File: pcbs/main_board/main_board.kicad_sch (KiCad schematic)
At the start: 2 parts, among them U1 mini_esp32, U2 ADXL345

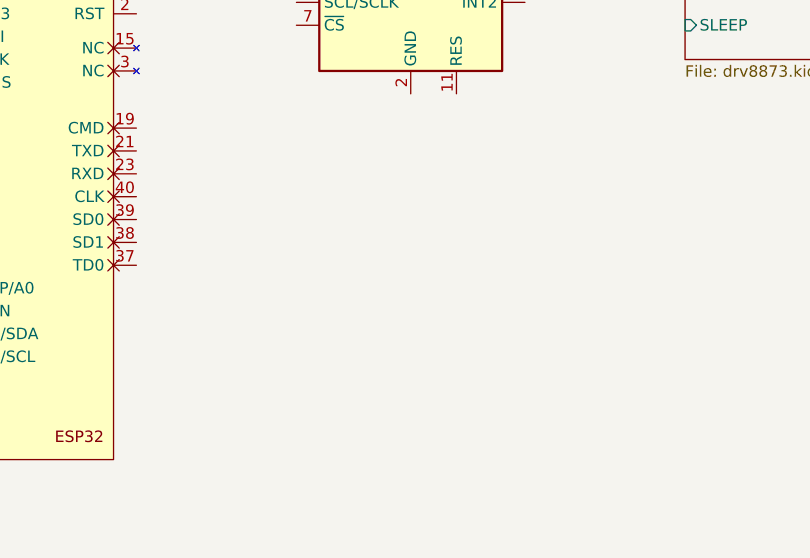
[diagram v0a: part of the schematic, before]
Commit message: Add display footprint, symbol
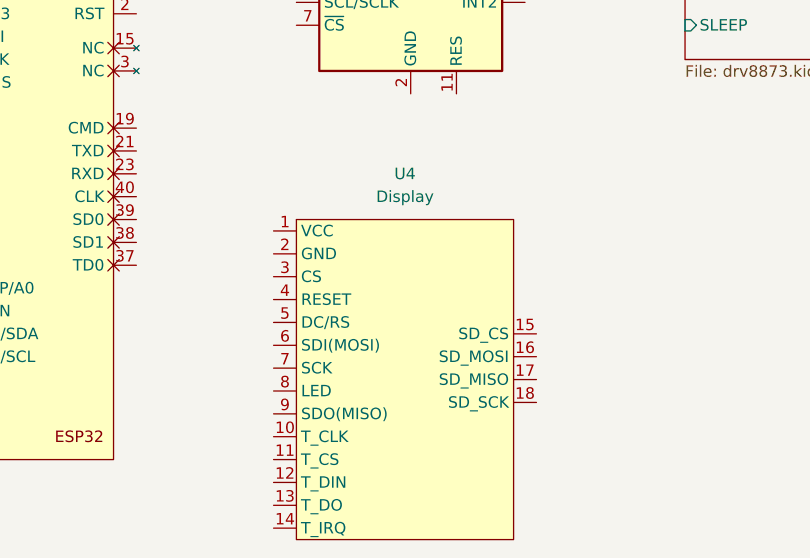
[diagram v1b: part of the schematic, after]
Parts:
- added U4: Display, display:display_footprint, symbol display_sym:display
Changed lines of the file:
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@@
 	(paper "A4")
+	(symbol
+		(lib_id "display_sym:display")
+		(at 99.06 88.9 0)
+		(unit 1)
+		(exclude_from_sim no)
+		(in_bom yes)
+		(on_board yes)
+		(dnp no)
+		(fields_autoplaced yes)
+		(property "Reference" "U4"
+			(at 98.425 67.31 0)
+			(effects
+				(font
+					(size 1.27 1.27)
+				)
+			)
+		)
+		(property "Value" "Display"
+			(at 98.425 69.85 0)
+			(effects
+				(font
+					(size 1.27 1.27)
+				)
+			)
+		)
+		(property "Footprint" "display:display_footprint"
+			(at 99.06 88.9 0)
+			(effects
+				(font
+					(size 1.27 1.27)
+				)
+				(hide yes)
+			)
+		)
+		(property "Datasheet" "https://www.lcdwiki.com/4.0inch_SPI_Module_ST7796"
+			(at 99.06 88.9 0)
+			(effects
+				(font
+					(size 1.27 1.27)
+				)
+				(hide yes)
+			)
+		)
+		(property "Description" "Display 4 inch"
+			(at 99.06 88.9 0)
+			(effects
+				(font
+					(size 1.27 1.27)
+				)
+				(hide yes)
+			)
+		)
+		(property "Manufacturer Part Number" "LA141073"
+			(at 99.06 88.9 0)
+			(effects
+				(font
+					(size 1.27 1.27)
+				)
+				(hide yes)
+			)
+		)
+		(property "Supplier" "LaskaKit"
+			(at 99.06 88.9 0)
+			(effects
+				(font
+					(size 1.27 1.27)
+				)
+				(hide yes)
+			)
+		)
+		(property "Supplier Part Number" "LA141073"
+			(at 99.06 88.9 0)
+			(effects
+				(font
+					(size 1.27 1.27)
+				)
+				(hide yes)
+			)
+		)
+		(pin "4"
+		)
+		(pin "9"
+		)
+		(pin "12"
+		)
+		(pin "14"
+		)
+		(pin "16"
+		)
+		(pin "2"
+		)
+		(pin "6"
+		)
+		(pin "8"
+		)
+		(pin "10"
+		)
+		(pin "1"
+		)
+		(pin "3"
+		)
+		(pin "5"
+		)
+		(pin "7"
+		)
+		(pin "11"
+		)
+		(pin "13"
+		)
+		(pin "15"
+		)
+		(pin "18"
+		)
+		(pin "17"
+		)
+		(instances
+			(project ""
+				(path "/86b00c07-962a-4c6d-8d05-813891e412c9"
+					(reference "U4")
+					(unit 1)
+				)
+			)
+		)
+	)
 	(symbol
 		(lib_id "Sensor_Motion:ADXL343")

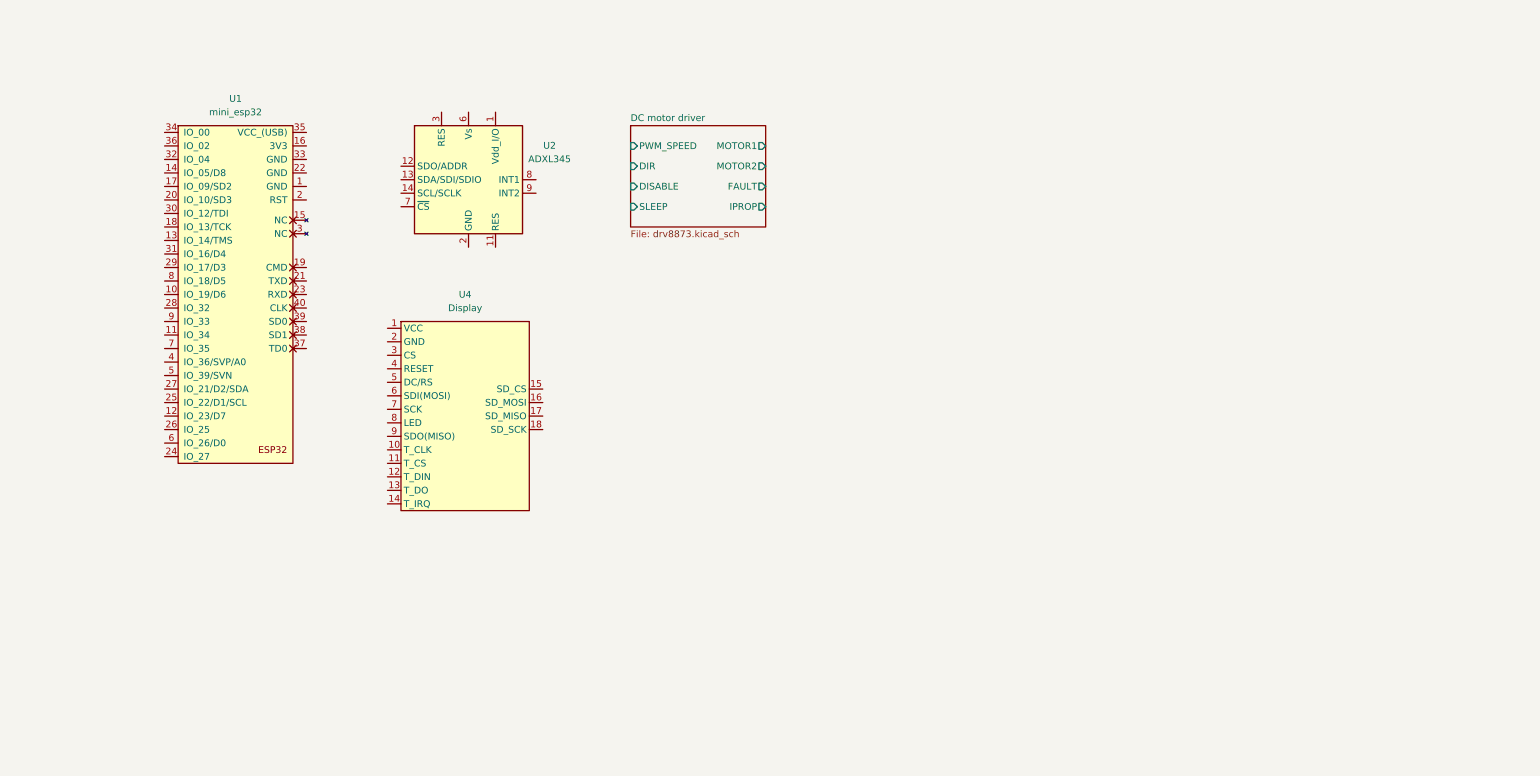
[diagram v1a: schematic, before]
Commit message: Add power distribution sheet
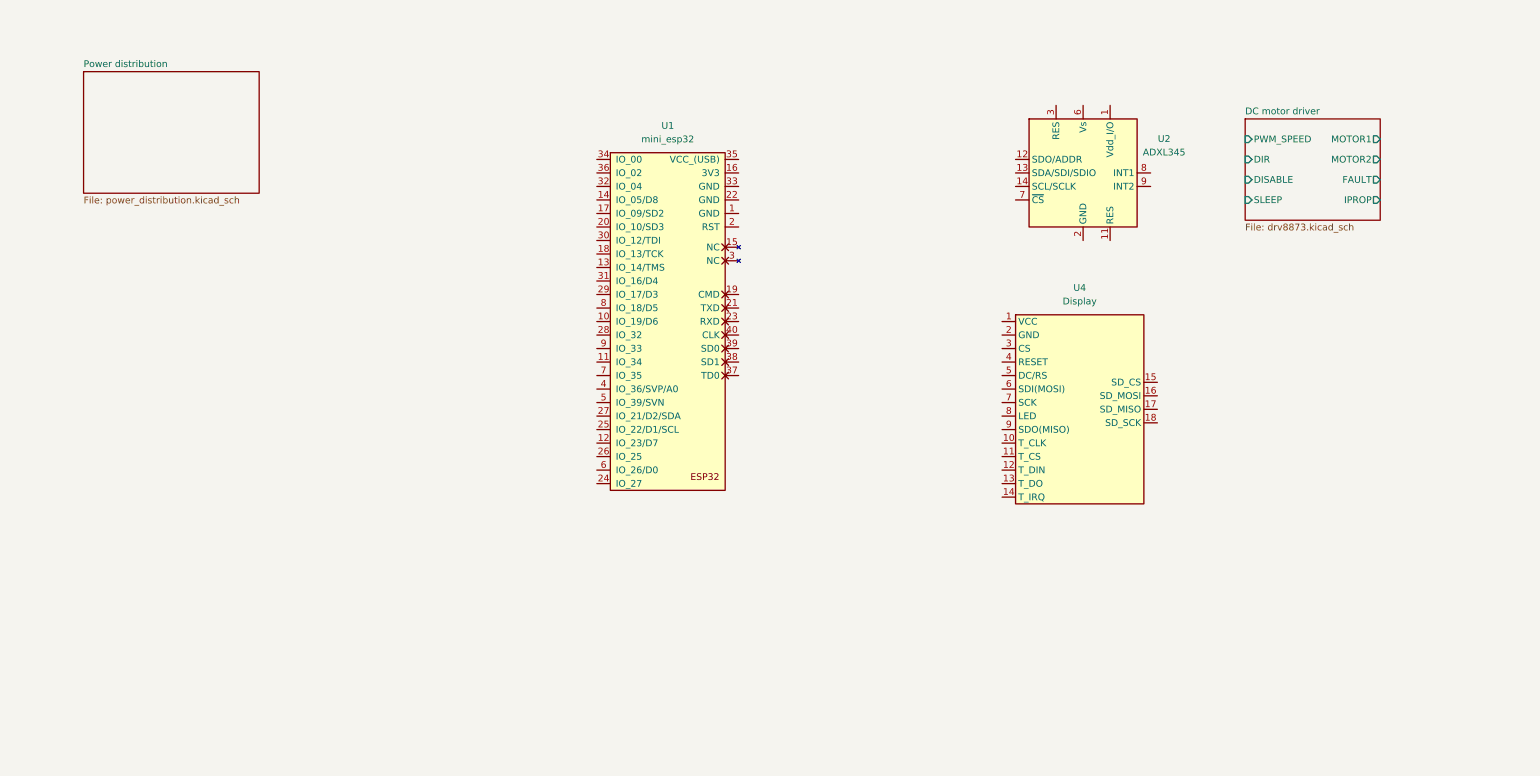
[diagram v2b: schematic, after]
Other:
- added sheet Power distribution (power_distribution.kicad_sch)
- moved on the sheet: U1, U2, U4
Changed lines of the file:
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@@
 	(symbol
 		(lib_id "display_sym:display")
-		(at 99.06 88.9 0)
+		(at 214.63 87.63 0)
 		(unit 1)
 		(exclude_from_sim no)
@@
 		(fields_autoplaced yes)
 		(property "Reference" "U4"
-			(at 98.425 67.31 0)
+			(at 213.995 66.04 0)
 			(effects
 				(font
@@
 		)
 		(property "Value" "Display"
-			(at 98.425 69.85 0)
+			(at 213.995 68.58 0)
 			(effects
 				(font
@@
 		)
 		(property "Footprint" "display:display_footprint"
-			(at 99.06 88.9 0)
+			(at 214.63 87.63 0)
 			(effects
 				(font
@@
 		)
 		(property "Datasheet" "https://www.lcdwiki.com/4.0inch_SPI_Module_ST7796"
-			(at 99.06 88.9 0)
+			(at 214.63 87.63 0)
 			(effects
 				(font
@@
 		)
 		(property "Description" "Display 4 inch"
-			(at 99.06 88.9 0)
+			(at 214.63 87.63 0)
 			(effects
 				(font
@@
 		)
 		(property "Manufacturer Part Number" "LA141073"
-			(at 99.06 88.9 0)
+			(at 214.63 87.63 0)
 			(effects
 				(font
@@
 		)
 		(property "Supplier" "LaskaKit"
-			(at 99.06 88.9 0)
+			(at 214.63 87.63 0)
 			(effects
 				(font
@@
 		)
 		(property "Supplier Part Number" "LA141073"
-			(at 99.06 88.9 0)
+			(at 214.63 87.63 0)
 			(effects
 				(font
@@
 	(symbol
 		(lib_id "Sensor_Motion:ADXL343")
-		(at 99.06 45.72 0)
+		(at 214.63 44.45 0)
 		(unit 1)
 		(exclude_from_sim no)
@@
 		(fields_autoplaced yes)
 		(property "Reference" "U2"
-			(at 114.3 39.2998 0)
+			(at 229.87 38.0298 0)
 			(effects
 				(font
@@
 		)
 		(property "Value" "ADXL345"
-			(at 114.3 41.8398 0)
+			(at 229.87 40.5698 0)
 			(effects
 				(font
@@
 		)
 		(property "Footprint" "Package_LGA:LGA-14_3x5mm_P0.8mm_LayoutBorder1x6y"
-			(at 99.06 45.72 0)
+			(at 214.63 44.45 0)
 			(effects
 				(font
@@
 		)
 		(property "Datasheet" "https://cz.mouser.com/datasheet/3/1014/1/5EB6D493A261F4A83E1FA0AE2BA84ED391EF50A03F09427C365C2A225C2ED909.pdf"
-			(at 99.06 45.72 0)
+			(at 214.63 44.45 0)
 			(effects
 				(font
@@
 		)
 		(property "Description" "3-Axis MEMS Accelerometer"
-			(at 99.06 45.72 0)
+			(at 214.63 44.45 0)
 			(effects
 				(font
@@
 		)
 		(property "Manufacturer Part Number" "ADXL345BCCZ"
-			(at 99.06 45.72 0)
+			(at 214.63 44.45 0)
 			(effects
 				(font
@@
 		)
 		(property "Supplier" "Mouser"
-			(at 99.06 45.72 0)
+			(at 214.63 44.45 0)
 			(effects
 				(font
@@
 		)
 		(property "Supplier Part Number" "584-ADXL345BCCZ"
-			(at 99.06 45.72 0)
+			(at 214.63 44.45 0)
 			(effects
 				(font
@@
 	(symbol
 		(lib_id "ESP32_mini:mini_esp32")
-		(at 54.61 34.29 0)
+		(at 135.89 39.37 0)
 		(unit 1)
 		(exclude_from_sim no)
@@
 		(fields_autoplaced yes)
 		(property "Reference" "U1"
-			(at 55.245 30.48 0)
+			(at 136.525 35.56 0)
 			(effects
 				(font
@@
 		)
 		(property "Value" "mini_esp32"
-			(at 55.245 33.02 0)
+			(at 136.525 38.1 0)
 			(effects
 				(font
@@
 		)
 		(property "Footprint" "ESP32_mini:ESP32_mini"
-			(at 58.42 31.75 0)
+			(at 139.7 36.83 0)
 			(effects
 				(font
@@
 		)
 		(property "Datasheet" "https://www.laskakit.cz/user/related_files/esp32-wroom-32_datasheet_en.pdf"
-			(at 58.42 31.75 0)
+			(at 139.7 36.83 0)
 			(effects
 				(font
@@
 		)
 		(property "Description" "ESP DevKit"
-			(at 54.61 34.29 0)
+			(at 135.89 39.37 0)
 			(effects
 				(font
@@
 		)
 		(property "Manufacturer Part Number" "~"
-			(at 54.61 34.29 0)
+			(at 135.89 39.37 0)
 			(effects
 				(font
@@
 		)
 		(property "Supplier" "LaskaKit"
-			(at 54.61 34.29 0)
+			(at 135.89 39.37 0)
 			(effects
 				(font
@@
 		)
 		(property "Supplier Part Number" "LA100089"
-			(at 54.61 34.29 0)
+			(at 135.89 39.37 0)
 			(effects
 				(font
@@
 	)
 	(sheet
-		(at 129.54 35.56)
+		(at 245.11 34.29)
 		(size 25.4 19.05)
 		(exclude_from_sim no)
@@
 		)
 		(property "Sheetname" "DC motor driver"
-			(at 129.54 34.8484 0)
+			(at 245.11 33.5784 0)
 			(effects
 				(font
@@
 		)
 		(property "Sheetfile" "drv8873.kicad_sch"
-			(at 129.54 55.1946 0)
+			(at 245.11 53.9246 0)
 			(effects
 				(font
@@
 		)
 		(pin "DIR" input
-			(at 129.54 43.18 180)
+			(at 245.11 41.91 180)
 			(effects
 				(font
@@
 		)
 		(pin "DISABLE" input
-			(at 129.54 46.99 180)
+			(at 245.11 45.72 180)
 			(effects
 				(font
@@
 		)
 		(pin "FAULT" output
-			(at 154.94 46.99 0)
+			(at 270.51 45.72 0)
 			(effects
 				(font
@@
 		)
 		(pin "IPROP" output
-			(at 154.94 50.8 0)
+			(at 270.51 49.53 0)
 			(effects
 				(font
@@
 		)
 		(pin "MOTOR1" output
-			(at 154.94 39.37 0)
+			(at 270.51 38.1 0)
 			(effects
 				(font
@@
 		)
 		(pin "MOTOR2" output
-			(at 154.94 43.18 0)
+			(at 270.51 41.91 0)
 			(effects
 				(font
@@
 		)
 		(pin "PWM_SPEED" input
-			(at 129.54 39.37 180)
+			(at 245.11 38.1 180)
 			(effects
 				(font
@@
 		)
 		(pin "SLEEP" input
-			(at 129.54 50.8 180)
+			(at 245.11 49.53 180)
 			(effects
 				(font
@@
 				)
 			)
+		)
+	)
+	(sheet
+		(at 26.67 25.4)
+		(size 33.02 22.86)
+		(exclude_from_sim no)
+		(in_bom yes)
+		(on_board yes)
+		(dnp no)
+		(fields_autoplaced yes)
+		(stroke
+			(width 0.1524)
+			(type solid)
+		)
+		(fill
+			(color 0 0 0 0.0000)
+		)
+		(property "Sheetname" "Power distribution"
+			(at 26.67 24.6884 0)
+			(effects
+				(font
+					(size 1.27 1.27)
+				)
+				(justify left bottom)
+			)
+		)
+		(property "Sheetfile" "power_distribution.kicad_sch"
+			(at 26.67 48.8446 0)
+			(effects
+				(font
+					(size 1.27 1.27)
+				)
+				(justify left top)
+			)
+		)
+		(instances
+			(project "main_board"
+				(path "/86b00c07-962a-4c6d-8d05-813891e412c9"
+					(page "3")
+				)
+			)

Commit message: Display wiring to esp
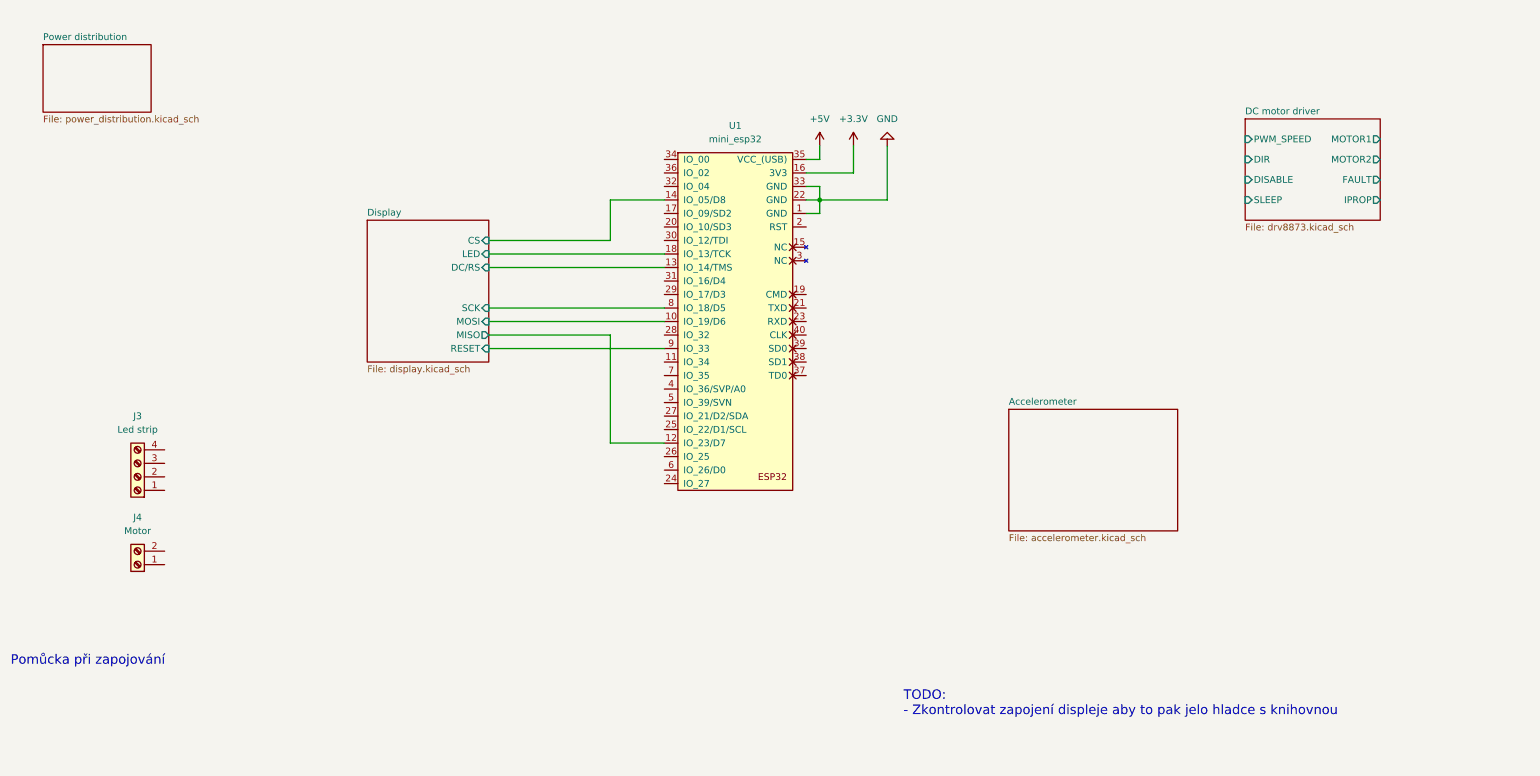
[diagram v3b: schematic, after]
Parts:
- removed U2: ADXL345, Package_LGA:LGA-14_3x5mm_P0.8mm_LayoutBorder1x6y, symbol Sensor_Motion:ADXL343
- removed U4: Display, display:display_footprint, symbol display_sym:display
- added J3: Led strip, symbol Connector:Screw_Terminal_01x04
- added J4: Motor, symbol Connector:Screw_Terminal_01x02
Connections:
- net GND: now reaches U1.1 (GND)
- net GND: now also U1.22 (GND), U1.33 (GND)
- net Display/MOSI: now reaches U1.10 (IO_19/D6)
- net Display/MISO: now reaches U1.12 (IO_23/D7)
- net Display/DC/RS: now reaches U1.13 (IO_14/TMS)
- net Display/CS: now reaches U1.14 (IO_05/D8)
- net +3.3V: now reaches U1.16 (3V3)
- net Display/LED: now reaches U1.18 (IO_13/TCK)
- net +5V: now reaches U1.35 (VCC_(USB))
- net Display/SCK: now reaches U1.8 (IO_18/D5)
- net Display/RESET: now reaches U1.9 (IO_33)
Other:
- added sheet Accelerometer (accelerometer.kicad_sch)
- added sheet Display (display.kicad_sch)
- note added: "Pomůcka při zapojování"
- note added: "TODO: - Zkontrolovat zapojení displeje aby to pak jelo hladce s knihovnou"
- moved on the sheet: U1

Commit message: Add led strip wiring
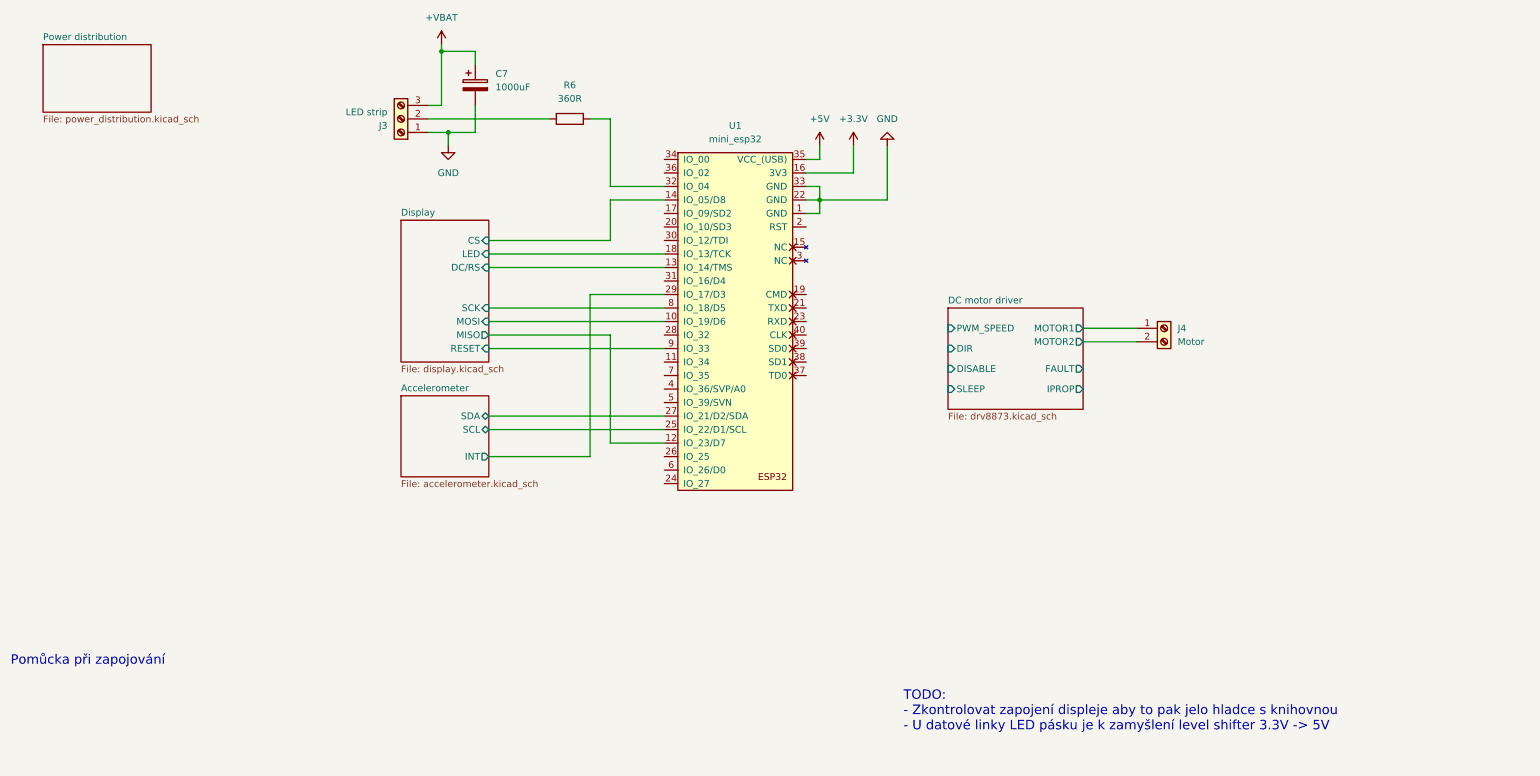
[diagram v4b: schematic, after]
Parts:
- removed J3: Led strip, symbol Connector:Screw_Terminal_01x04
- added C7: 1000uF, symbol Device:C_Polarized
- added J3: LED strip, symbol Connector:Screw_Terminal_01x03
- added R6: 360R, Resistor_SMD:R_0603_1608Metric_Pad0.98x0.95mm_HandSolder, symbol Device:R
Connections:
- net DC motor driver/MOTOR1: now also J4.1 (Pin_1)
- net DC motor driver/MOTOR2: now also J4.2 (Pin_2)
- net GND: now also C7.2, J3.1 (Pin_1)
- net Accelerometer/SCL: now reaches U1.25 (IO_22/D1/SCL)
- net Accelerometer/SDA: now reaches U1.27 (IO_21/D2/SDA)
- net Accelerometer/INT: now reaches U1.29 (IO_17/D3)
- net at U1.32 (IO_04): now also R6.1
- new net: J3.2 (Pin_2), R6.2
- new net +VBAT: C7.1, J3.3 (Pin_3)
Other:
- sheet Accelerometer ports: added INT, SCL, SDA; removed none
- note added: "TODO: - Zkontrolovat zapojení displeje aby to pak jelo hladce s knihovnou - U datové linky LED pásku je k zamyšlení level shifter 3.3V -> 5V"
- note removed: "TODO: - Zkontrolovat zapojení displeje aby to pak jelo hladce s knihovnou"
- moved on the sheet: J4
